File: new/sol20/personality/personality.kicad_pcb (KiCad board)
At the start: 2 copper layers, 44.4 x 96.5 mm, 17 parts, among them J1 Personality-connector, SW1 SW_DIP_x05, U1 74HC00, U2 28C256

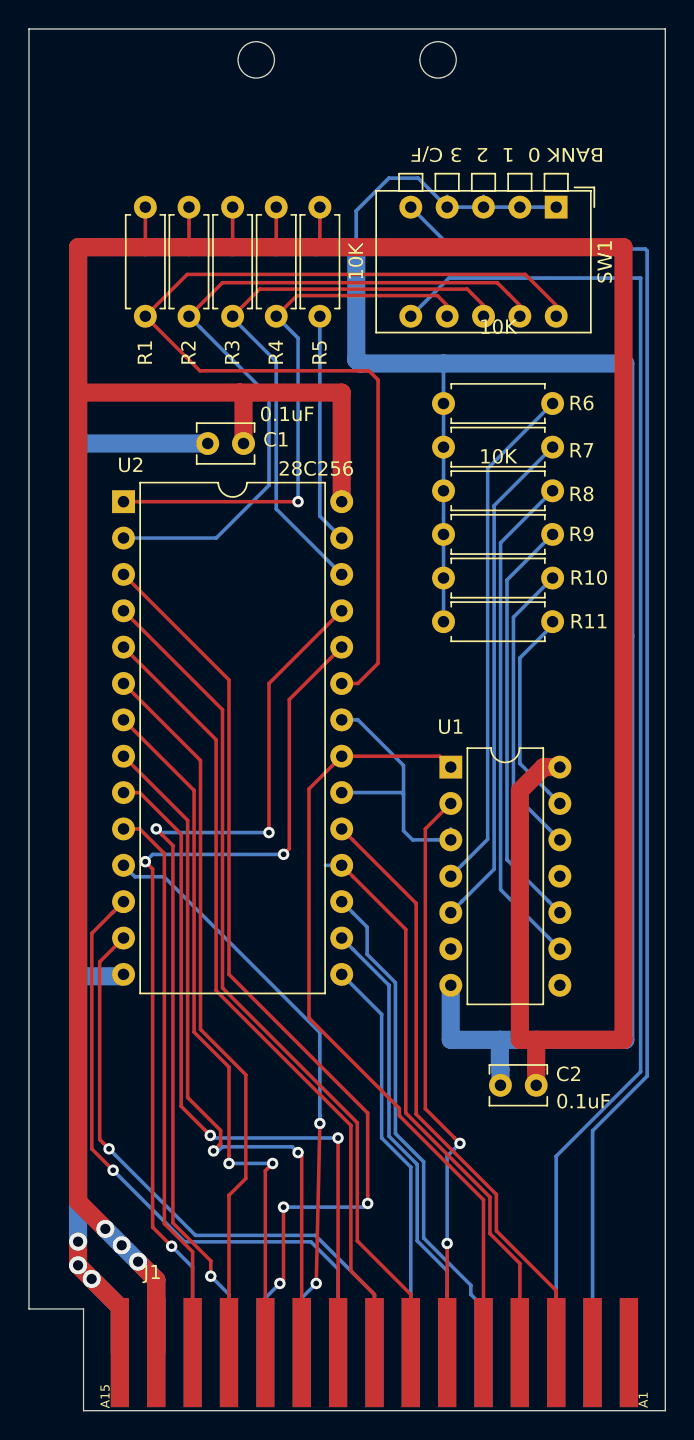
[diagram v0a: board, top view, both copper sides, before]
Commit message: update 502 files to fix missing traces
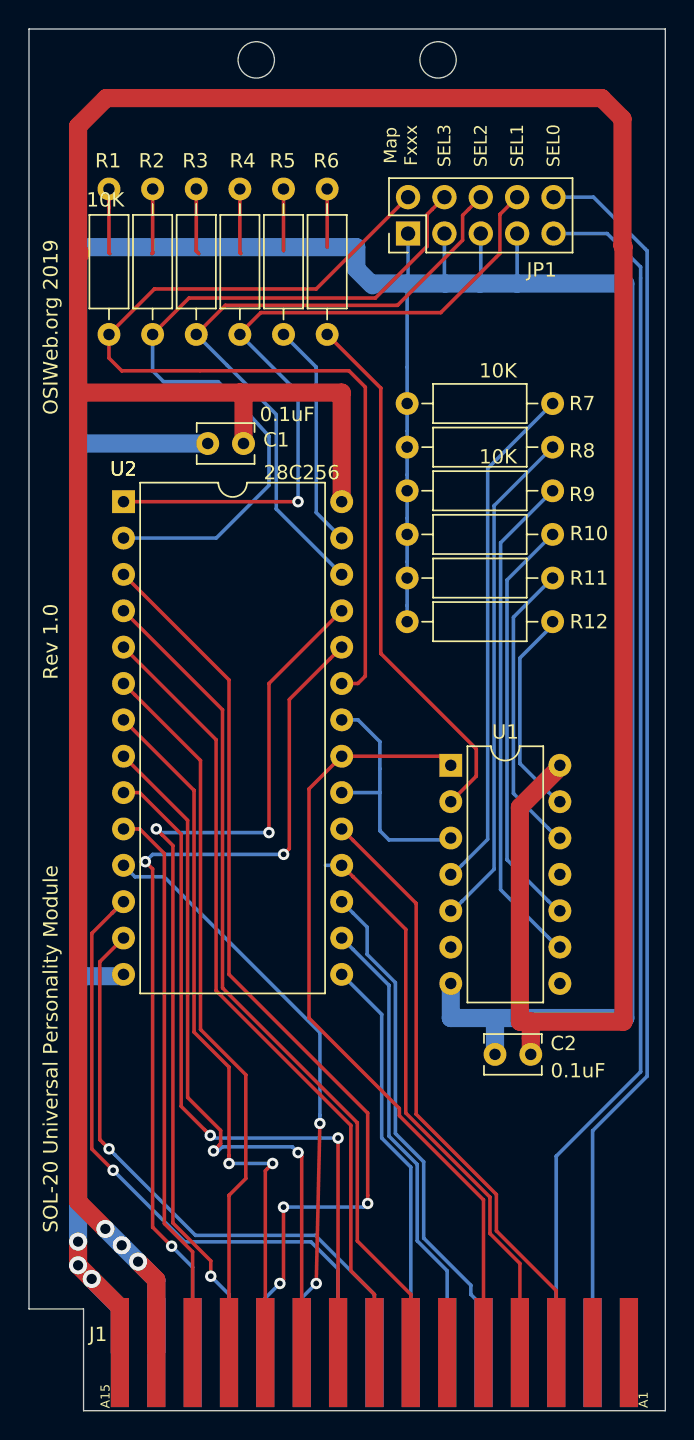
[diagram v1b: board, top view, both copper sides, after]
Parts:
- removed the R11 at (151.9, 93.0)
- removed SW1: SW_DIP_x05, Button_Switch_THT:SW_DIP_SPSTx05_Piano_CTS_Series194-5MSTN_W7.62mm_P2.54mm
- added JP1: JP_block_5, Connector_PinHeader_2.54mm:PinHeader_2x05_P2.54mm_Vertical, F.Cu at (141.8, 65.8)
- added R10: 10K, Resistor_THT:R_Axial_DIN0207_L6.3mm_D2.5mm_P10.16mm_Horizontal, F.Cu at (151.9, 86.9)
- added R12: 10K, Resistor_THT:R_Axial_DIN0207_L6.3mm_D2.5mm_P10.16mm_Horizontal, F.Cu at (151.9, 93.0)
- R1, R2, R3, R4, R5, R6, R7, R8, R9: footprint Resistor_THT:R_Axial_DIN0207_L6.3mm_D2.5mm_P7.62mm_Horizontal -> Resistor_THT:R_Axial_DIN0207_L6.3mm_D2.5mm_P10.16mm_Horizontal
- R11: renamed from R10; footprint Resistor_THT:R_Axial_DIN0207_L6.3mm_D2.5mm_P7.62mm_Horizontal -> Resistor_THT:R_Axial_DIN0207_L6.3mm_D2.5mm_P10.16mm_Horizontal
- U1: value 74HC00 -> 74LS08
- moved R6 16.5 mm to (136.1, 72.9), turned to 90 degrees
- moved R7 3.05 mm to (151.9, 77.7)
- moved R9 3.05 mm to (151.9, 83.8)
- moved R8 3.05 mm to (151.9, 80.8)
- moved R1 2.84 mm to (120.9, 72.9)
- moved R2 2.84 mm to (124.0, 72.9)
- moved R3 2.84 mm to (127.0, 72.9)
- moved R4 2.84 mm to (130.0, 72.9)
- moved R5 2.84 mm to (133.1, 72.9)
- moved C2 2.19 mm to (150.4, 123.2)
- moved U1 0.13 mm to (144.8, 103.0)
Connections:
- R6 pad 1: Net-(R6-Pad1) -> /~C4
- R6 pad 2: GND -> +5V
- U1 pad 10: Net-(R9-Pad1) -> Net-(R10-Pad1)
- U1 pad 4: Net-(R6-Pad1) -> Net-(R7-Pad1)
- U1 pad 5: Net-(R7-Pad1) -> Net-(R8-Pad1)
- U1 pad 9: Net-(R8-Pad1) -> Net-(R9-Pad1)
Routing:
- net Net-(R6-Pad1): track 36.0 -> 0.00 mm
- net Net-(R10-Pad1): track 0.00 -> 29.3 mm
- net +5V: track 254.9 -> 282.4 mm
- net /BKSEL_3: track 38.6 -> 50.5 mm
- net Net-(J1-PadB2): track 96.3 -> 86.6 mm
- net Net-(J1-PadB3): track 94.7 -> 85.3 mm
- net Net-(R9-Pad1): track 29.3 -> 35.2 mm
- net /BKSEL_2: track 40.0 -> 45.8 mm
- net GND: track 247.5 -> 242.1 mm
- net /BKSEL_0: track 71.8 -> 67.3 mm
- net /BKSEL_1: track 50.6 -> 53.4 mm
- net /~C4: track 40.5 -> 37.7 mm, vias 2 -> 0
- net Net-(U1-Pad3): track 18.9 -> 17.4 mm
- net Net-(R7-Pad1): track 35.5 -> 36.0 mm
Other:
- board text added: "Map Fxxx"
- board text added: "OSIWeb.org 2019"
- board text added: "Rev 1.0"
- board text added: "SEL0"
- board text added: "SEL1"
- board text added: "SEL2"
- board text added: "SEL3"
- board text added: "SOL-20 Universal Personality Module"
- board text removed: "BANK 0 1 2 3 C/F"

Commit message: - Replaced DIP switch with 0.1" 8x2 header.  Cheaper, smaller, more reliable - Replaced discrete resistors with resistor networks - Added jumper to select between 27C256 EPROMs and all other allowed EPROM/EEPROM variants (27C64,27C128,28C64,28C128,28C256) - Last two pins of jumper header may be used to plug in a header from the main board for FXXX remapping, to avoid having to access the bottom of the main SOL PCB. - Removed the C4xx disable option.
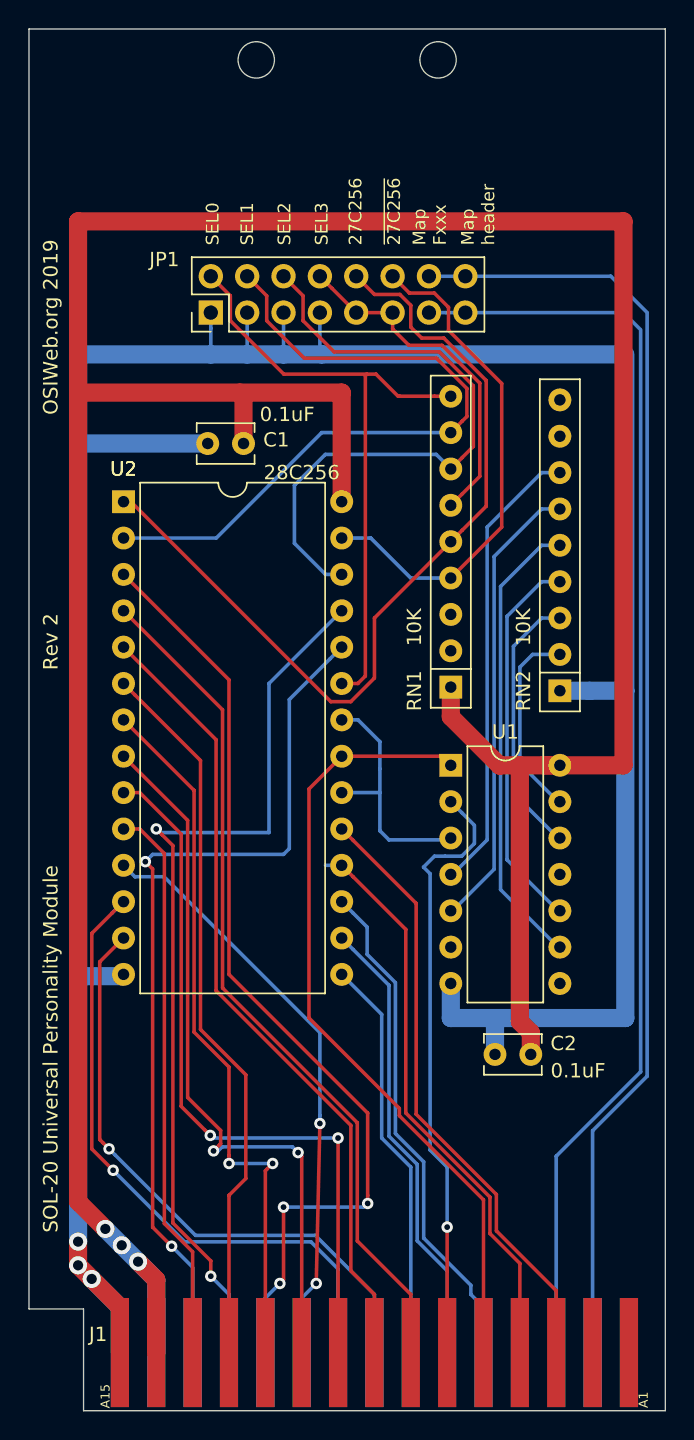
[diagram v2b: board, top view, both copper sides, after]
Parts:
- removed R1, R10, R11, R12, R2, R3, R4, R5, R6, R7, R8, R9: 10K, Resistor_THT:R_Axial_DIN0207_L6.3mm_D2.5mm_P10.16mm_Horizontal
- added RN1: 10K, Resistor_THT:R_Array_SIP9, F.Cu at (144.8, 97.5)
- added RN2: 10K, Resistor_THT:R_Array_SIP9, F.Cu at (152.4, 97.8)
- JP1: value JP_block_5 -> JP_block_8; footprint Connector_PinHeader_2.54mm:PinHeader_2x05_P2.54mm_Vertical -> Connector_PinHeader_2.54mm:PinHeader_2x08_P2.54mm_Vertical
- moved JP1 14.8 mm to (128.0, 71.4)
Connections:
- JP1 pad 10: Net-(J1-PadB2) -> Net-(JP1-Pad10)
- JP1 pad 9: Net-(J1-PadB3) -> /BKSEL_3
- U2 pad 1: /BKSEL_3 -> Net-(JP1-Pad10)
- U2 pad 27: Net-(R5-Pad1) -> Net-(JP1-Pad12)
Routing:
- net Net-(JP1-Pad10): track 0.00 -> 61.0 mm
- net +5V: track 282.4 -> 230.8 mm
- net GND: track 242.1 -> 206.0 mm
- net Net-(JP1-Pad12): track 0.00 -> 35.5 mm
- net /BKSEL_3: track 50.5 -> 24.3 mm, vias 1 -> 0
- net /BKSEL_0: track 67.3 -> 44.3 mm
- net Net-(R5-Pad1): track 15.9 -> 0.00 mm
- net /~C4: track 37.7 -> 42.4 mm, vias 0 -> 1
- net /BKSEL_1: track 53.4 -> 49.1 mm
- net Net-(J1-PadB2): track 86.6 -> 90.5 mm
- net Net-(RN2-Pad7): track 36.0 -> 32.1 mm
- net Net-(J1-PadB3): track 85.3 -> 89.1 mm
- net Net-(RN2-Pad6): track 35.5 -> 32.1 mm
- net Net-(RN2-Pad5): track 35.2 -> 32.4 mm
- net Net-(RN2-Pad4): track 29.3 -> 26.9 mm
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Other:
- board text added: "27C256"
- board text added: "Map header"
- board text added: "Rev 2"
- board text added: "~27C256"
- board text removed: "Rev 1.0"

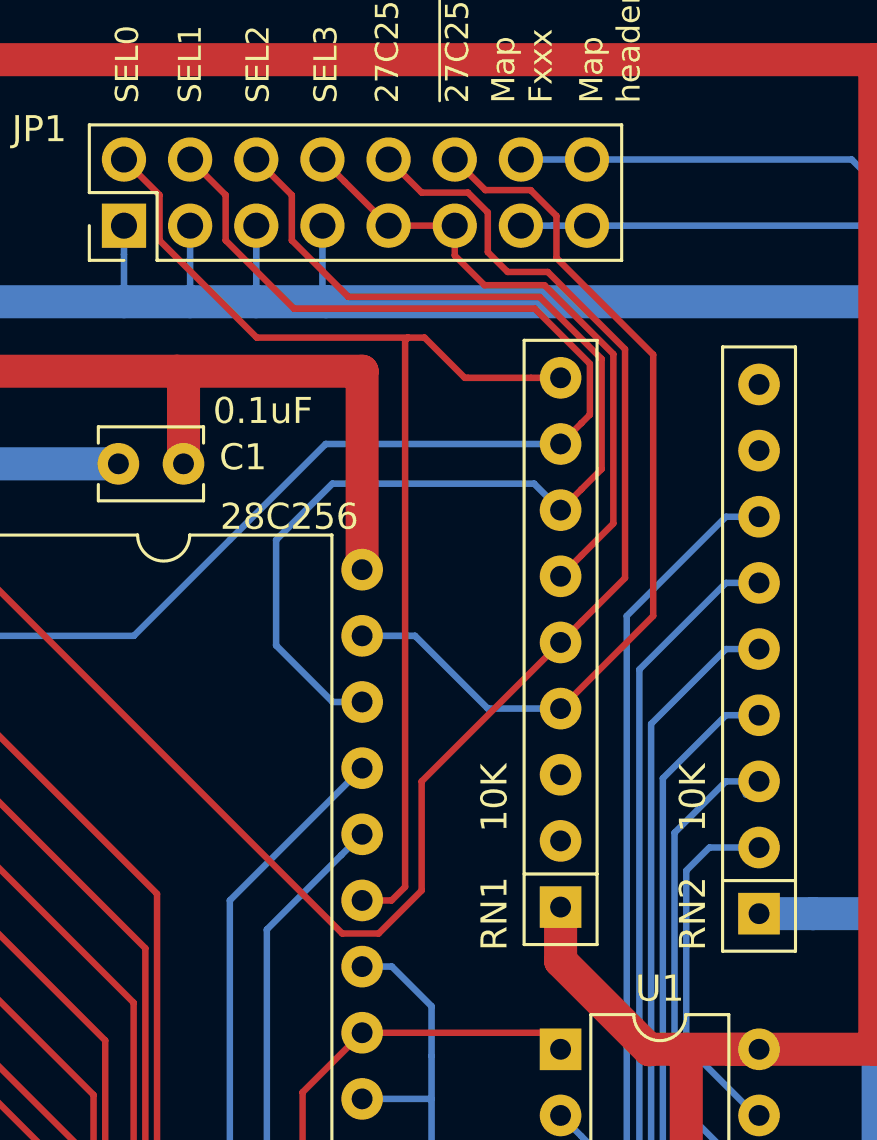
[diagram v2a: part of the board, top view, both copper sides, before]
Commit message: use pins 1-7 on RN1, so shorter 6 and 7 resistor networks can be used in place.
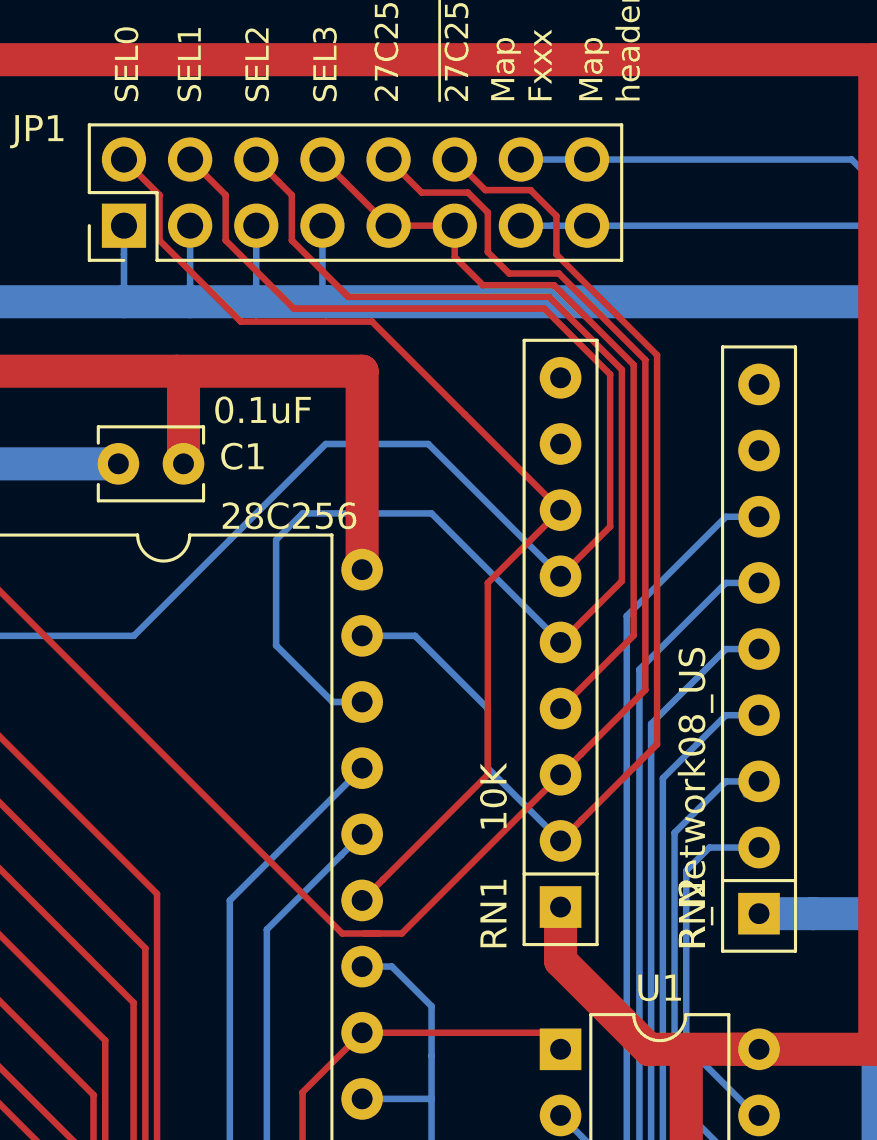
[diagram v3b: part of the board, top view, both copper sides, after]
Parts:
- RN2: value 10K -> R_Network08_US
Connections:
- RN1 pad 2: Net-(RN1-Pad2) -> Net-(JP1-Pad12)
- RN1 pad 3: Net-(RN1-Pad3) -> Net-(JP1-Pad10)
- RN1 pad 4: Net-(JP1-Pad12) -> /BKSEL_3
- RN1 pad 5: Net-(JP1-Pad10) -> /BKSEL_2
- RN1 pad 6: /BKSEL_3 -> /BKSEL_1
- RN1 pad 7: /BKSEL_2 -> /BKSEL_0
- RN1 pad 8: /BKSEL_1 -> Net-(RN1-Pad8)
- RN1 pad 9: /BKSEL_0 -> Net-(RN1-Pad9)
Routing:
- net Net-(JP1-Pad12): track 35.5 -> 44.2 mm
- net /BKSEL_1: track 49.1 -> 57.1 mm
- net /BKSEL_2: track 44.4 -> 51.5 mm
- net /BKSEL_3: track 24.3 -> 30.3 mm
- net /BKSEL_0: track 44.3 -> 41.5 mm
- net Net-(JP1-Pad10): track 61.0 -> 62.9 mm

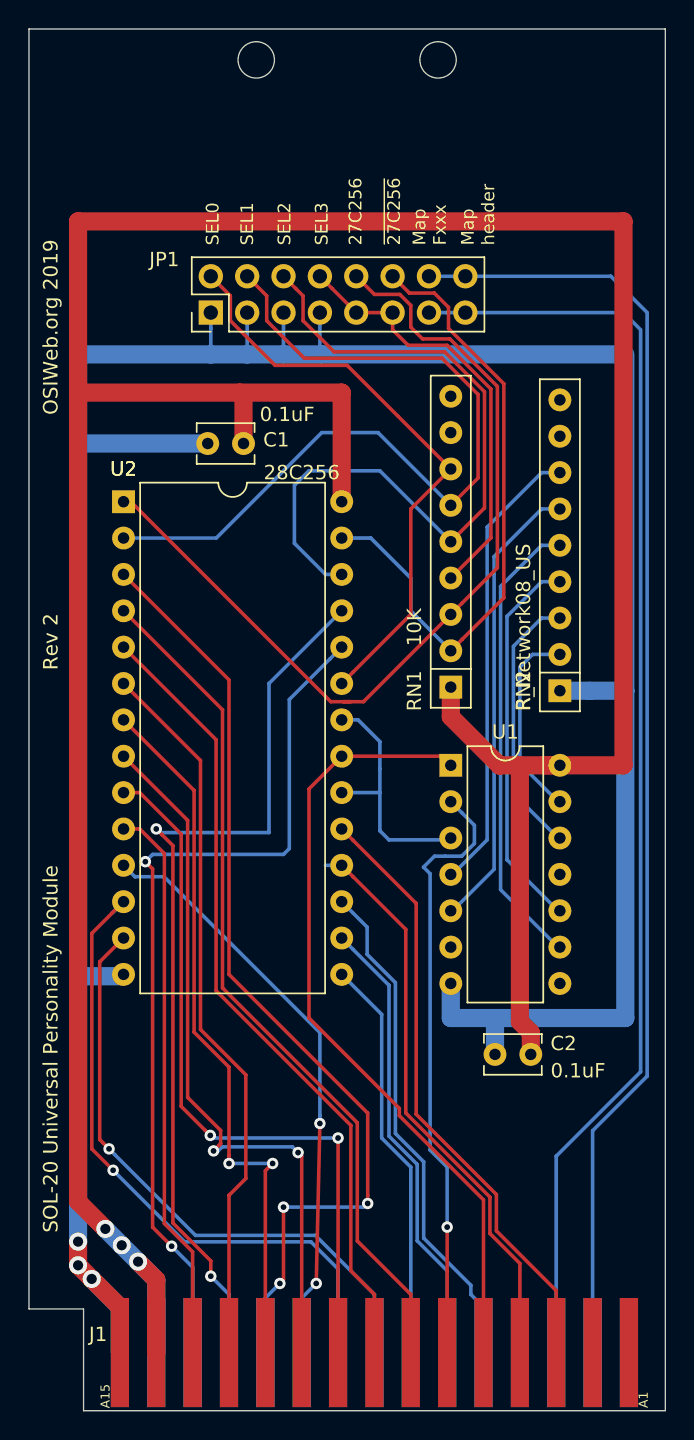
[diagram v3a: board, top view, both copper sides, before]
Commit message: moved 5V rail from under silk screen
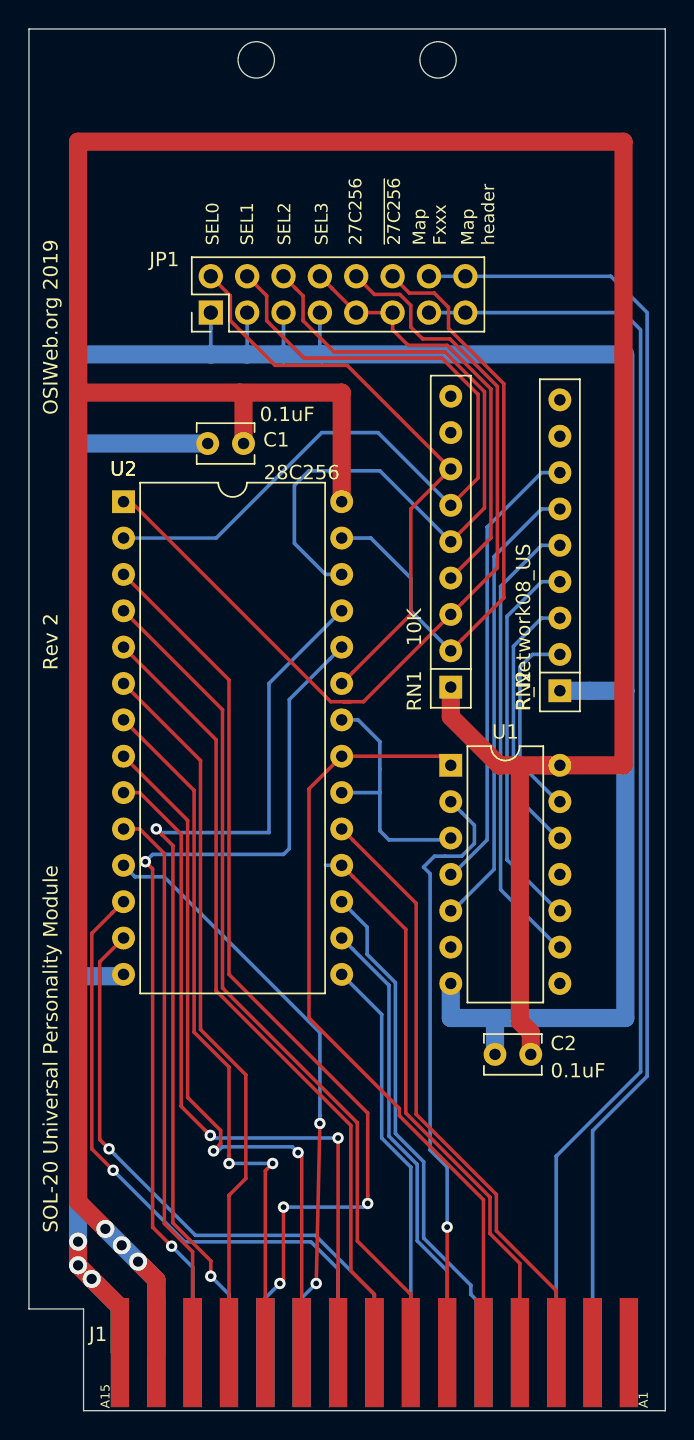
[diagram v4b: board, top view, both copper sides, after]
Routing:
- net +5V: track 230.8 -> 241.9 mm
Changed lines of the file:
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@@
   (segment (start 137.16 84.582) (end 137.16 76.962) (width 1.27) (layer F.Cu) (net 2))
   (segment (start 130.302 80.518) (end 130.302 77.216) (width 1.27) (layer F.Cu) (net 2))
-  (segment (start 120.65 135.382) (end 118.745 133.477) (width 1.27) (layer F.Cu) (net 2))
   (segment (start 130.048 76.962) (end 118.745 76.962) (width 1.27) (layer F.Cu) (net 2))
-  (segment (start 118.745 133.477) (end 118.745 65) (width 1.27) (layer F.Cu) (net 2))
   (segment (start 144.78 97.536) (end 144.78 99.606) (width 1.27) (layer F.Cu) (net 2))
   (segment (start 152.4 102.997) (end 151.26863 102.997) (width 1.27) (layer F.Cu) (net 2))
@@
   (segment (start 150.368 121.666) (end 149.606 120.904) (width 1.27) (layer F.Cu) (net 2))
   (segment (start 150.368 123.19) (end 150.368 121.666) (width 1.27) (layer F.Cu) (net 2))
-  (segment (start 156.845 102.997) (end 156.845 65) (width 1.27) (layer F.Cu) (net 2))
-  (segment (start 152.4 102.997) (end 156.845 102.997) (width 1.27) (layer F.Cu) (net 2))
-  (segment (start 118.745 65) (end 156.845 65) (width 1.27) (layer F.Cu) (net 2))
+  (segment (start 156.845 102.997) (end 152.4 102.997) (width 1.27) (layer F.Cu) (net 2))
+  (segment (start 118.745 59.436) (end 156.845 59.436) (width 1.27) (layer F.Cu) (net 2))
+  (segment (start 156.845 59.436) (end 156.845 102.997) (width 1.27) (layer F.Cu) (net 2))
+  (segment (start 118.745 133.477) (end 118.745 59.436) (width 1.27) (layer F.Cu) (net 2))
+  (segment (start 120.65 135.382) (end 118.745 133.477) (width 1.27) (layer F.Cu) (net 2))
   (segment (start 144.78 108.204) (end 140.462 108.204) (width 0.254) (layer B.Cu) (net 5))
   (segment (start 139.827 101.346) (end 139.827 103.251) (width 0.254) (layer B.Cu) (net 5))
